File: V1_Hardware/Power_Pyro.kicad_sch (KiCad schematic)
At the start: 36 parts, among them J2 Screw_Terminal_01x04, J3 Screw_Terminal_01x04, Q1 IRLML6344TRPBF, Q2 IRLML6344TRPBF, SW2 SW_SPDT, U2 AP2112K-3.3, U3 MP2393GTL-Z, U4 AP20P30Q, U5 AP20P30Q

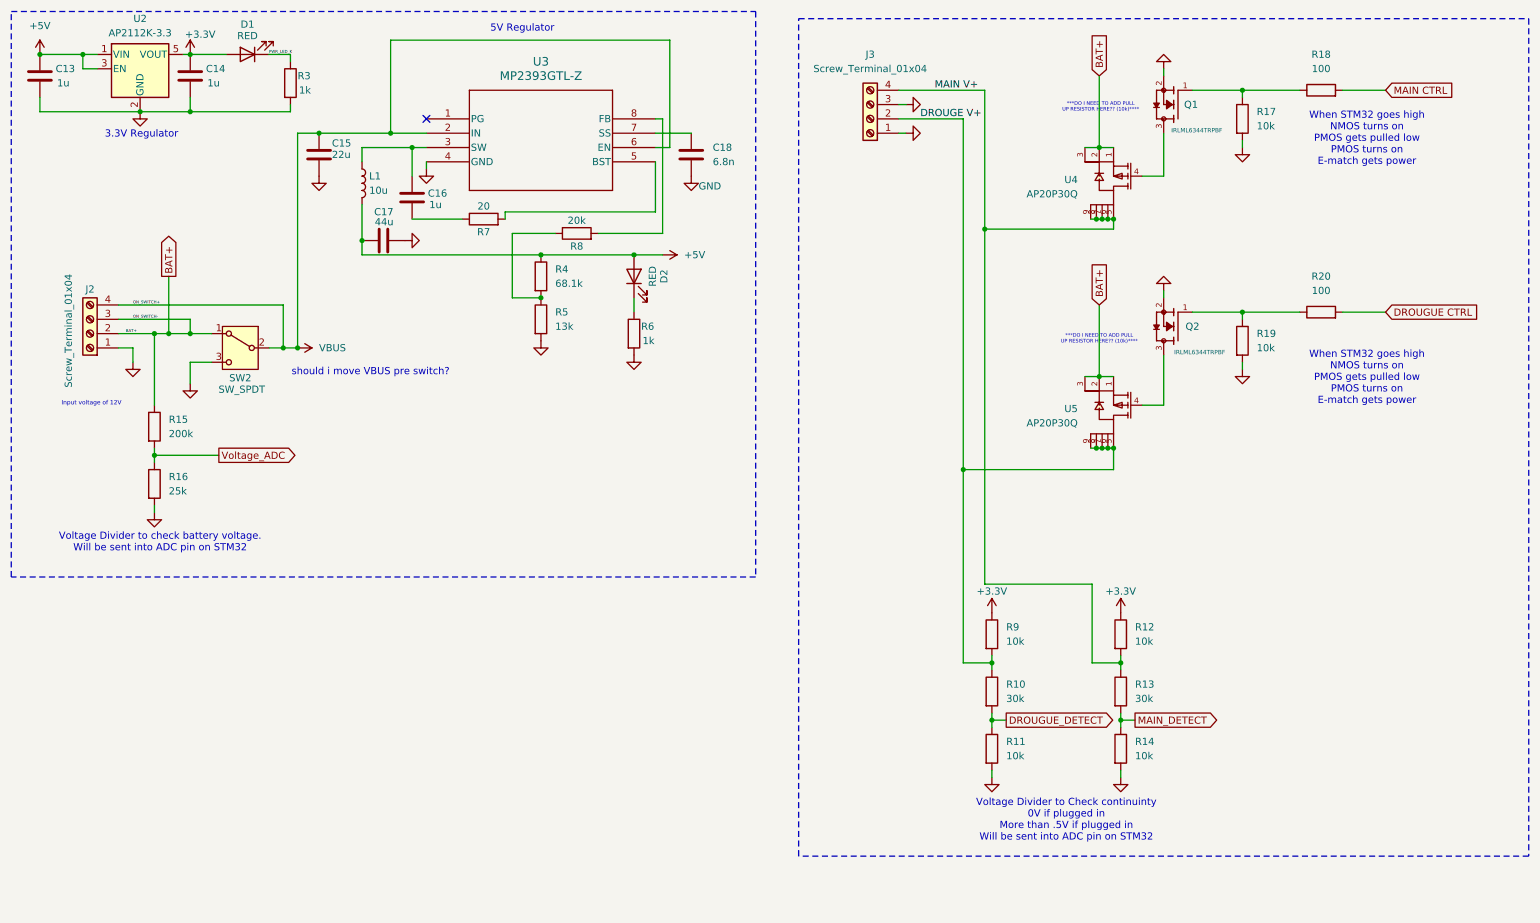
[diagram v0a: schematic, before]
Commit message: added the V1 to personal repo from org repo
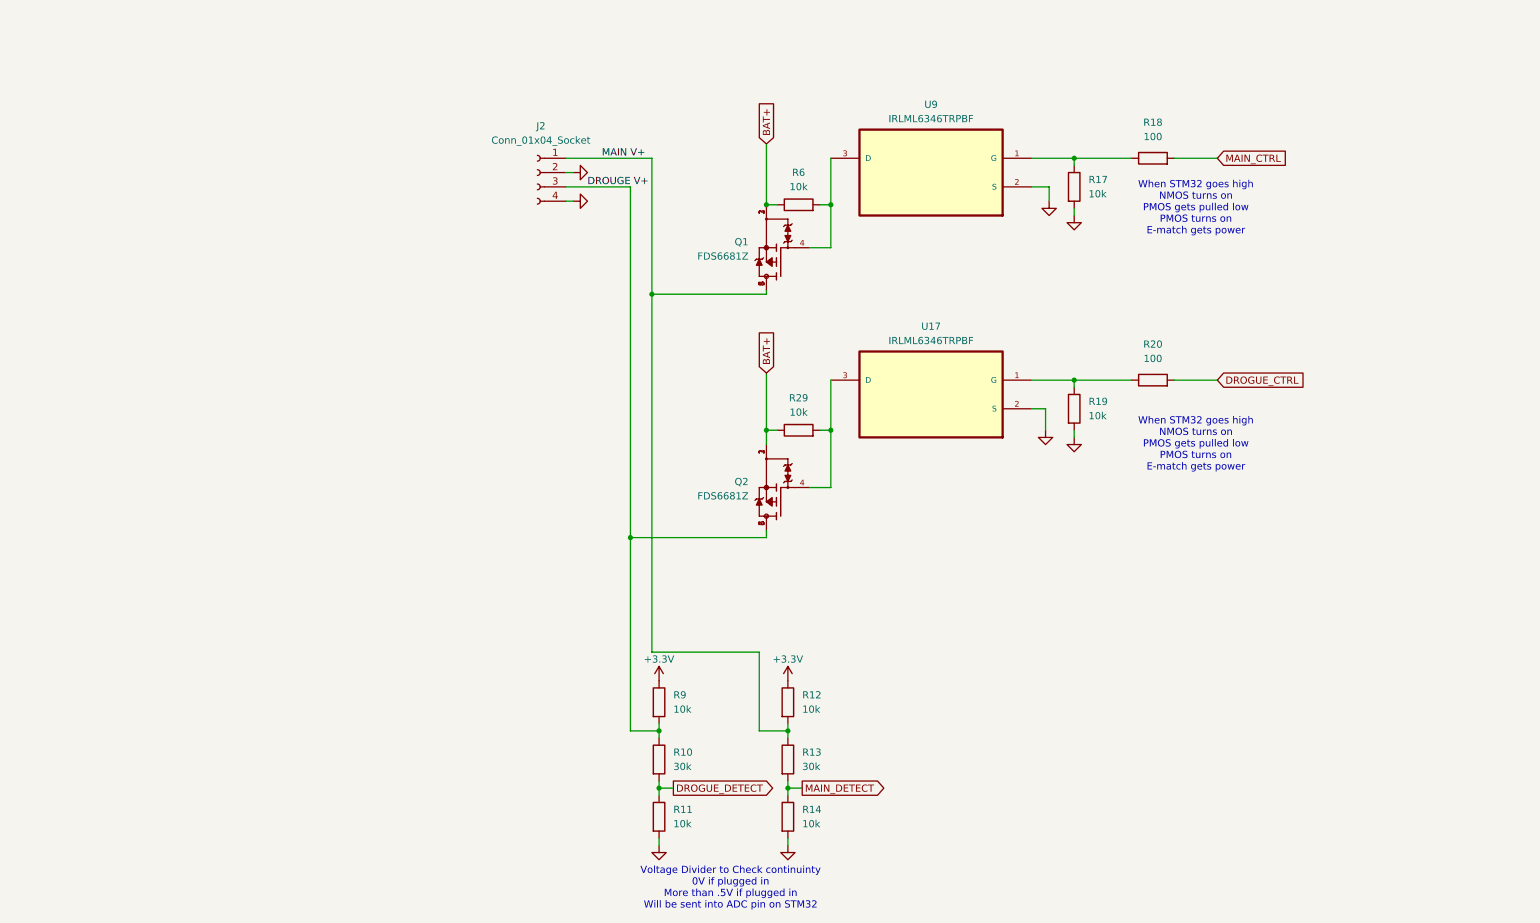
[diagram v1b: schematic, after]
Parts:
- removed C13, C14, C16: 1u, symbol Device:C
- removed C15: 22u, symbol Device:C
- removed C17: 44u, symbol Device:C
- removed C18: 6.8n, symbol Device:C
- removed D1, D2: RED, symbol Device:LED
- removed J2, J3: Screw_Terminal_01x04, symbol Connector:Screw_Terminal_01x04
- removed L1: 10u, symbol Device:L
- removed Q1, Q2: IRLML6344TRPBF, IRLML6344TRPBF:TRANS_IRLML6344TRPBF, symbol IRLML6344TRPBF:IRLML6344TRPBF
- removed R15: 200k, symbol Device:R
- removed R16: 25k, symbol Device:R
- removed R3: 1k, symbol Device:R
- removed R4: 68.1k, symbol Device:R
- removed R5: 13k, symbol Device:R
- removed R7: 20, symbol Device:R
- removed R8: 20k, symbol Device:R
- removed SW2: SW_SPDT, symbol Switch:SW_SPDT
- removed U2: AP2112K-3.3, Package_TO_SOT_SMD:SOT-23-5, symbol Regulator_Linear:AP2112K-3.3
- removed U3: MP2393GTL-Z, SOT583_MP2393, symbol MP2393GTL-Z:MP2393GTL-Z
- removed U4, U5: AP20P30Q, polaris-fp:DFN-8_L3.3-W3.0-P0.65-LS3.3-BL-EP, symbol polaris-sym:AP20P30Q
- added J2: Conn_01x04_Socket, Connector_Molex:Molex_Nano-Fit_105309-xx04_1x04_P2.50mm_Vertical, symbol Connector:Conn_01x04_Socket
- added Q1, Q2: FDS6681Z, V1:FDS6681Z, symbol FDS6681Z:FDS6681Z
- added R29: 10k, Resistor_SMD:R_0603_1608Metric_Pad0.98x0.95mm_HandSolder, symbol Device:R
- added U17, U9: IRLML6346TRPBF, V1:IRLML6346TRPBF, symbol IRLML6346TRPBF:IRLML6346TRPBF
- R10, R11, R12, R13, R14, R17, R18, R19, R20, R9: footprint (none) -> Resistor_SMD:R_0603_1608Metric_Pad0.98x0.95mm_HandSolder
- R6: value 1k -> 10k; footprint (none) -> Resistor_SMD:R_0603_1608Metric_Pad0.98x0.95mm_HandSolder
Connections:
- net BAT+: now also R6.1, Q1.1, Q1.2, Q1.3, Q2.1, Q2.2, Q2.3, R29.1
- net DROUGE V+: now also J2.3 (Pin_3), Q2.5, Q2.6, Q2.7, Q2.8
- net GND: now also J2.2 (Pin_2), J2.4 (Pin_4), U17.2 (S), U9.2 (S); no longer R6.2
- net MAIN V+: now also J2.1 (Pin_1), Q1.5, Q1.6, Q1.7, Q1.8
- net at R19.1, R20.1: now also U17.1 (G)
- net at R17.1, R18.1: now also U9.1 (G)
- net DROUGUE CTRL renamed DROGUE_CTRL
- net DROUGUE_DETECT renamed DROGUE_DETECT
- net MAIN CTRL renamed MAIN_CTRL
- new net: Q2.4, R29.2, U17.3 (D)
- new net: Q1.4, R6.2, U9.3 (D)
- no-connect marks 1 -> 0
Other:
- note removed: "***DO I NEED TO ADD PULL UP RESISTOR HERE?? (10k)****"
- note removed: "3.3V Regulator"
- note removed: "5V Regulator"
- note removed: "Input voltage of 12V"
- note removed: "Voltage Divider to check battery voltage. Will be sent into ADC pin on STM32"
- note removed: "should i move VBUS pre switch?"
- moved on the sheet: R10, R11, R12, R13, R14, R17, R18, R19, R20, R9
